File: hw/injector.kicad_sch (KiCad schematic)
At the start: 49 parts, among them Q401 150V N-ch, logic-level, Q402 150V N-ch, 18A peak, Q403 60V N-ch, 18A, Q404 150V N-ch, 18A peak, Q405 60V N-ch, 18A, Q406 150V N-ch, 18A peak, Q407 60V small-signal, Q408 150V N-ch, 18A peak, Q409 60V small-signal, Q410 150V N-ch, 18A peak, Q411 60V small-signal, U401 TPS40210

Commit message: Choose the gate drivers: AUIRS2181S on all eight gates, for having no interlock
Infineon AUIRS2181(4)S, datasheet retrieved and text-extracted. Its
first listed typical application is "Piezo / common rail Injection."

THE DECIDING PROPERTY IS ONE A PARAMETRIC SEARCH WOULD NEVER FILTER FOR:
no cross-conduction interlock (the datasheet's own feature table: 2181
"no", 2183/2184 "yes"). In a half bridge, HO and LO together is
shoot-through and every driver prevents it -- so the reflex is that a
driver WITHOUT interlock is the less safe choice. In an injector stage
the "high" and "low" switches are not a half bridge. They are in series
with the coil and must BOTH be on for it to conduct at all. UCC27282-Q1
and UCC27712-Q1 have interlock and could not fire an injector.

It also clears the two ratings the obvious 120 V candidate fails, and
both are now executable in run_sim.py:

  UCC27211A-Q1 HB absolute maximum 120 V, against a bank node at
  103.8 V worst case plus 12 V of VB -- 4.1 V of headroom on an
  absolute maximum. AUIRS2181S: 625 V, 5.4x.

  UCC27211A-Q1 HS DC minimum -1 V, against D_fw dropping the bank node
  1.0-1.3 V below ground on EVERY hold off-time -- violated in normal
  operation, not in a fault. AUIRS2181S operates to -5 V, clear by
  3.7 V.

Five in use: four on injector, each pairing one high side with one low
side by package rather than by circuit, and one on metering_egr for its
low side, so the board carries one gate-driver part number.

THE KILL PATH MOVES TO HIN. The part has no shutdown pin and a
ground-referenced FET cannot short a gate floating 100 V up -- but HIN
is ground-referenced, so supervisor.cir's kill FET goes there behind a
1k from the MCU. Slower than the low-side gate clamp (330 ns max driver
turn-off against 23 ns), which is acceptable because it is not the path
the fail-safe argument rests on: the low sides are in series with every
coil, and killing any one stops that cylinder.

12V_GATE, A RAIL THE BOARD DID NOT HAVE. The driv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
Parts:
- removed D407: 150V 20A ultrafast, symbol Device:D
- removed Q406: 150V N-ch, 18A peak, symbol Device:Q_NMOS_GSD
- removed Q407: 60V small-signal, symbol Device:Q_NMOS_GSD
- added C408, C409, C410, C411, C412, C413, C414, C415: 1uF 25V, symbol Device:C
- added C416: 10uF 25V, symbol Device:C
- added D407: 13V, symbol Device:D_Zener
- added D410, D411, D412, D413, D414: 150V 20A ultrafast, symbol Device:D
- added Q406: NPN 160V, DPAK, symbol Device:Q_NPN_BCE
- added Q407: NPN small-signal, symbol Device:Q_NPN_BCE
- added Q412, Q414, Q416: 150V N-ch, 18A peak, symbol Device:Q_NMOS_GSD
- added Q413, Q415, Q417: 60V small-signal, symbol Device:Q_NMOS_GSD
- added R421, R423, R424, R425: 470R, symbol Device:R
- added R422: 100k, symbol Device:R
- added R426, R427: 5mOhm 2W 1%, symbol Device:R
- added U402, U403, U404, U405: AUIRS2181S, Package_SO:SOIC-8_3.9x4.9mm_P1.27mm, symbol ecu25kva:AUIRS2181S
- D403, D405: value 150V 20A ultrafast -> 200V 1A fast; Note BLOCKING, not freewheeling. Without it the battery FET's ow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 -> Bootstrap diode -- the driver has none built in. Blocks VB,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; Tag INJ-RECIRC -> (none)
- D404, D406: value 150V 20A ultrafast -> 200V 1A fast; Note Anode to GROUND, cathode to the bank node. This is the slow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 -> Bootstrap diode -- the driver has none built in. Blocks VB,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; Source injector_turnoff.cir D_fw -> (none); Tag INJ-RECIRC -> (none)
- D408: Note Low side back into the boost reservoir. NOT a Zener active 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 -> BLOCKING, not freewheeling. Without it the battery FET's ow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; Peak 28.7 W instantaneous during turn-off, ~8x the 3.6 W average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 -> (none); Source injector_turnoff.cir Drc -- the diode memo 10 recommends an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 -> (none); Tag (none) -> INJ-RECIRC
- D409: Note Low side back into the boost reservoir. NOT a Zener active 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 -> Anode to GROUND, cathode to the bank node. This is the slow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; Peak 28.7 W instantaneous during turn-off, ~8x the 3.6 W average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 -> (none); Source injector_turnoff.cir Drc -- the diode memo 10 recommends an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 -> injector_turnoff.cir D_fw; Tag (none) -> INJ-RECIRC
- Q402: value 150V N-ch, 18A peak -> 60V small-signal; Note Bank-shared: cylinders 1 and 3 fire 240 crank degrees apart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 -> Pulls HIN low against a hung MCU driving it high through th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; Source injector_boost.cir -- the 100 V branch; injector_turnoff.ci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 -> supervisor.cir -- the kill FET, moved to the driver's logic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; Vds 150 V class against a 100 V rail the recirculation bump can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 -> (none)
- Q403, Q405: value 60V N-ch, 18A -> 60V small-signal; Note Chops for hold. 60 V class, not 150 V: the series blocking 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 -> Pulls HIN low against a hung MCU driving it high through th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; Source boost_converter.cir arrangement A -- hold current comes fro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 -> supervisor.cir -- the kill FET, moved to the driver's logic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; Vds 60 V -> (none)
- Q404: value 150V N-ch, 18A peak -> 60V small-signal; Note One cylinder in this bank. Kept as a separate switch rather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 -> Pulls HIN low against a hung MCU driving it high through th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; Source injector_boost.cir -- the 100 V branch; injector_turnoff.ci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 -> supervisor.cir -- the kill FET, moved to the driver's logic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; Vds 150 V class against a 100 V rail the recirculation bump can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 -> (none)
- Q408: Note Cylinder 3. Independent per channel -- the high side is ban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 -> Bank-shared: cylinders 1 and 3 fire 240 crank degrees apart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; Source injector_turnoff.cir Sls (Ron 20 mOhm) -> injector_boost.cir -- the 100 V branch; injector_turnoff.ci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; Vds 150 V class: at turn-off this drain is driven above the 100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 -> 150 V class against a 100 V rail the recirculation bump can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
- Q409, Q411: value 60V small-signal -> 60V N-ch, 18A; Note In parallel with the 470 ohm pulldown, not instead of it. R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 -> Chops for hold. 60 V class, not 150 V: the series blocking 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; Source supervisor.cir -- the kill FET -> boost_converter.cir arrangement A -- hold current comes fro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; Vds (none) -> 60 V
- Q410: Note Cylinder 2. Independent per channel -- the high side is ban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 -> One cylinder in this bank. Kept as a separate switch rather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; Source injector_turnoff.cir Sls (Ron 20 mOhm) -> injector_boost.cir -- the 100 V branch; injector_turnoff.ci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; Vds 150 V class: at turn-off this drain is driven above the 100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 -> 150 V class against a 100 V rail the recirculation bump can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
- R410, R411, R413: value 470R -> 1k; Note A pulldown to GROUND here would hold Vgs at minus the bank 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 -> Between the MCU and HIN, so the kill FET below can override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; Source supervisor.cir claim 6, referenced to SOURCE rather than to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 -> (none)
- R412: value 100k -> 1k; Note Bleed. With both high sides off and the low sides off, noth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 -> Between the MCU and HIN, so the kill FET below can override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
- R414: value 470R -> 47k; Note A pulldown to GROUND here would hold Vgs at minus the bank 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 -> Zener bias, split in two so neither resistor carries the fu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; Source supervisor.cir claim 6, referenced to SOURCE rather than to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 -> (none)
- R415: value 100k -> 47k; Note Bleed. With both high sides off and the low sides off, noth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 -> Second half.
- R416: value 470R -> 56R; Cost 21.3 mA per gate at 10 V; 1.28 W across all six -> (none); Note Largest standard value holding the gate under Vgs(th)=1.0 V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 -> The limit's sense resistor. 0.28 V drop at the 5 mA design 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; Source supervisor.cir claim 6; bom_requirements GATE-PULLDOWN -> (none)
- R417, R418: Cost 21.3 mA per gate at 10 V; 1.28 W across all six -> (none); Note Largest standard value holding the gate under Vgs(th)=1.0 V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 -> A pulldown to GROUND here would hold Vgs at minus the bank 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; Source supervisor.cir claim 6; bom_requirements GATE-PULLDOWN -> supervisor.cir claim 6, referenced to SOURCE rather than to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
- R419: value 5mOhm 2W 1% -> 100k; Note Bank A, cylinders 1 and 3 sharing one return. They fire 240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 -> Bleed. With both high sides off and the low sides off, noth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; Power 1.62 W at peak, but ~1.25% duty per cylinder at 1500 rpm -> (none); Signal 90 mV at the 18 A peak, 50 mV at the 10 A hold -- too small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 -> (none); Source settled on this sheet -- docs/pinmap.md sec.1.6 asked for t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 -> (none)
- R420: value 5mOhm 2W 1% -> 470R; Note Bank B, cylinder 2 alone. Drawn as its own shunt rather tha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 -> A pulldown to GROUND here would hold Vgs at minus the bank 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; Power 1.62 W at peak, but ~1.25% duty per cylinder at 1500 rpm -> (none); Signal 90 mV at the 18 A peak, 50 mV at the 10 A hold -- too small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 -> (none); Source settled on this sheet -- docs/pinmap.md sec.1.6 asked for t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 -> supervisor.cir claim 6, referenced to SOURCE rather than to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
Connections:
- net BOOST_100V: now also Q408.3 (D), Q410.3 (D), R414.1, D412.1 (K), D413.1 (K), D414.1 (K), Q406.2 (C); no longer D408.1 (K), D409.1 (K), Q402.3 (D), Q404.3 (D)
- net GATE_KILL: now also Q402.1 (G), Q403.1 (G), Q404.1 (G), Q405.1 (G), Q413.1 (G), Q415.1 (G), Q417.1 (G); no longer Q409.1 (G), Q411.1 (G)
- net GND: now also D409.2 (A), Q402.2 (S), Q403.2 (S), Q404.2 (S), Q405.2 (S), C409.2, C411.2, C413.2, C415.2, C416.2, D407.2 (A), D411.2 (A), Q413.2 (S), Q415.2 (S), Q417.2 (S), R422.2, R423.2, R424.2, R425.2, R426.2, R427.2, U402.3 (COM), U403.3 (COM), U404.3 (COM), U405.2 (LIN), U405.3 (COM); no longer D404.2 (A), D406.2 (A), Q409.2 (S), Q411.2 (S), R412.2, R415.2, R416.2, R417.2, R418.2, R420.2
- net HSA_BAT_GATE: now also Q409.1 (G), R418.1, U403.7 (HO); no longer Q403.1 (G), R411.1
- net HSA_BOOST_GATE: now also Q408.1 (G), R417.1, U402.7 (HO); no longer Q402.1 (G), R410.1
- net HSB_BAT_GATE: now also Q411.1 (G), R421.1, U405.7 (HO); no longer Q405.1 (G), R414.1
- net HSB_BOOST_GATE: now also Q410.1 (G), R420.1, U404.7 (HO); no longer Q404.1 (G), R413.1
- net INJ_A_03: now also D409.1 (K), Q408.2 (S), Q409.2 (S), R417.2, R418.2, R419.1, C408.2, C410.2, U402.6 (VS), U403.6 (VS); no longer D404.1 (K), Q402.2 (S), Q403.2 (S), R410.2, R411.2, R412.1
- net INJ_B_05: now also Q410.2 (S), Q411.2 (S), R420.2, C412.2, C414.2, D411.1 (K), R421.2, R422.1, U404.6 (VS), U405.6 (VS); no longer D406.1 (K), Q404.2 (S), Q405.2 (S), R413.2, R414.2, R415.1
- net INJ_HS_A: now also R410.1
- net INJ_HS_A_BAT: now also R411.1
- net INJ_HS_B: now also R412.1
- net INJ_HS_B_BAT: now also R413.1
- net INJ_LS1_73: now also D412.2 (A), Q412.3 (D)
- net INJ_LS2_29: now also D414.2 (A), Q416.3 (D); no longer D409.2 (A), Q410.3 (D)
- net INJ_LS3_07: now also D413.2 (A), Q414.3 (D); no longer D408.2 (A), Q408.3 (D)
- net INJ_LS_1: now also U402.2 (LIN)
- net INJ_LS_2: now also U404.2 (LIN)
- net INJ_LS_3: now also U403.2 (LIN)
- net ISNS_INJ_A_SENSE: now also Q412.2 (S), Q414.2 (S), R426.1; no longer Q408.2 (S), R419.1
- net ISNS_INJ_B_SENSE: now also Q416.2 (S), R427.1; no longer Q410.2 (S), R420.1
- net LS1_GATE: now also Q412.1 (G), Q413.3 (D), R423.1, U402.4 (LO); no longer R416.1
- net LS2_GATE: now also Q416.1 (G), Q417.3 (D), R425.1, U404.4 (LO); no longer Q410.1 (G), Q411.3 (D), R418.1
- net LS3_GATE: now also Q414.1 (G), Q415.3 (D), R424.1, U403.4 (LO); no longer Q408.1 (G), Q409.3 (D), R417.1
- net VBAT_PROT: now also D408.2 (A), D410.2 (A); no longer D403.2 (A), D405.2 (A)
- net UB1_VB: now reaches D405.1 (K)
- net UB1_VB: now also C412.1, U404.8 (VB); no longer Q405.3 (D)
- net UA1_VB: now reaches D403.1 (K)
- net UA1_VB: now also C408.1, U402.8 (VB); no longer Q403.3 (D)
- new net: D410.1 (K), Q411.3 (D)
- new net: D408.1 (K), Q409.3 (D)
- new net: R414.2, R415.1
- new net 12V_GATE: C409.1, C411.1, C413.1, C415.1, C416.1, D403.2 (A), D404.2 (A), D405.2 (A), D406.2 (A), Q407.3 (E), R416.2, U402.5 (VCC), U403.5 (VCC), U404.5 (VCC), U405.5 (VCC)
- new net BASE_12V: D407.1 (K), Q406.1 (B), Q407.2 (C), R415.2
- new net Q1E_12V: Q406.3 (E), Q407.1 (B), R416.1
- new net UA1_HIN: Q402.3 (D), R410.2, U402.1 (HIN)
- new net UA2_HIN: Q403.3 (D), R411.2, U403.1 (HIN)
- new net UA2_VB: C410.1, D404.1 (K), U403.8 (VB)
- new net UB1_HIN: Q404.3 (D), R412.2, U404.1 (HIN)
- new net UB2_HIN: Q405.3 (D), R413.2, U405.1 (HIN)
- new net UB2_VB: C414.1, D406.1 (K), U405.8 (VB)
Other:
- note added: "12V_GATE -- gate-drive supply for every driver on the board, from the boost rail so it survives cranking"
- note added: "GATE DRIVERS -- AUIRS2181S x4. Each pairs one high side with one low side; the pairing is by package, not by circuit."
- note added: "GATE DRIVERS: AUIRS2181S x4, chosen 21 Sep 2026. Its first listed application is 'Piezo / common rail Injection', and three properties decided it, each against a part that failed on it. NO CROSS-CONDUCTION INTERLOCK: in a half bridge HO and LO together is shoot-through, but here the high and low switches are in SERIES with the coil and must BOTH be on to fire it -- UCC27282-Q1 and UCC27712-Q1 hav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"
- note added: "GATE_KILL reaches the four high sides at the drivers' HIN inputs, not at the gates -- a ground-referenced kill FET cannot short a gate floating 100 V up, but HIN is ground-referenced. See the gate-driver block on the right."
- note removed: "GATE_KILL reaches the four high sides through the driver's own SHUTDOWN input, not through a clamp -- a ground-referenced kill FET cannot short a gate that floats 100 V up. Nothing is drawn for it here because the driver is not chosen; see the note at the foot of the sheet."
- note removed: "PARTS NOT CHOSEN ON THIS SHEET. Seven gate drivers and two current-sense amplifiers, on the same named-net treatment power_input gives its two controller gates. LOW-SIDE DRIVERS (LS1/LS2/LS3_DRV_IN -> *_GATE). Output impedance <= 25 ohm, from supervisor.cir claim 2: the 470 ohm pulldown is not a perturbation on the driver, it is the bottom half of a divider with it, and at 100 ohm the gate reache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"

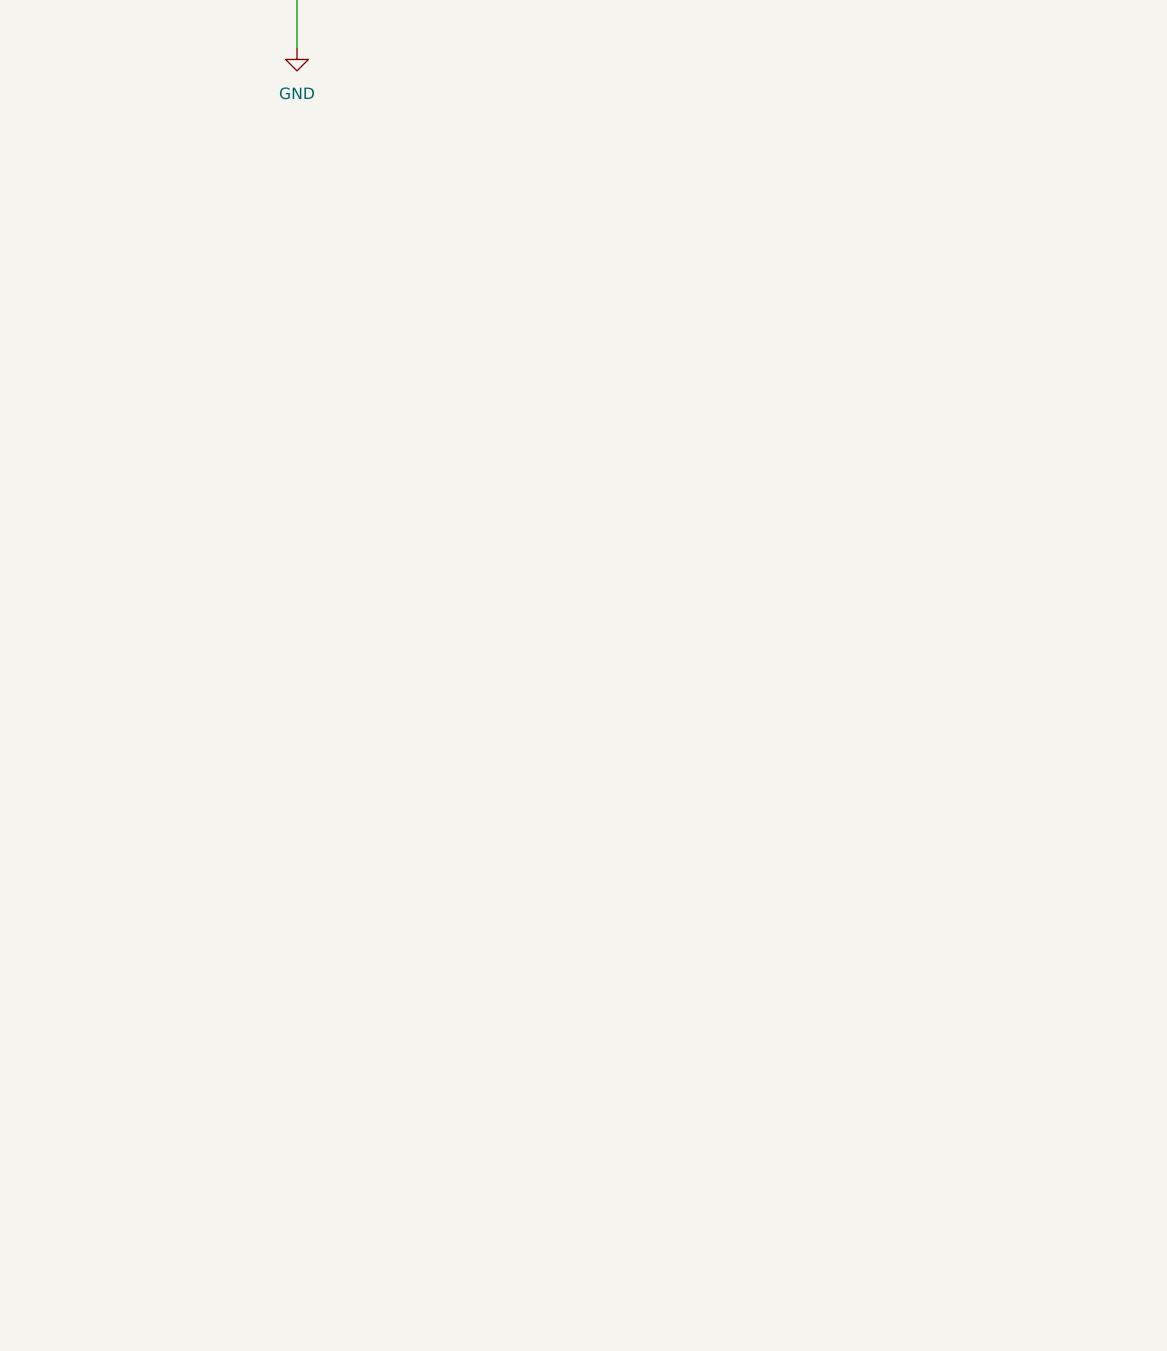
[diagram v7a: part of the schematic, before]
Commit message: Choose the current-sense amplifiers: INA181A1-Q1 on all three channels
TI SLYS018F, retrieved and text-extracted. VCM -0.2 V to 26 V, so it
sits across a ground-referenced shunt; gain 20; 350 kHz; +/-150 uV
offset at VCM = 0.

One part, one gain, three channels, and the gain is set for the
injector: 5 mOhm x 18 A x 20 = 1.80 V at the peak, 1.00 V at the 10 A
hold, leaving headroom to 3.28 V -- so a fault current up to 32.8 A is
MEASURED rather than clipped, which is what an overcurrent check needs.
The metering channel takes the same gain and reads its 0.675 A setpoint
at 675 mV, 844 counts.

Supplied from 3V3_MCU, which makes the output ADC-safe by construction:
it cannot swing above VS - 0.02 V, so these three channels need no
3.3 V zener at the MCU pin, unlike every channel on sensors_analog.

Closes MU-ISENSE's open half -- that tag specified the 50 mOhm shunt and
said the amplifier was not optional. The Kelvin-tap layout requirement
is carried in each amplifier's own field.

Also redrawn: the metering FET, placed at rot=270 since 20 September.
At 270 the drain and source sit side by side and every wire to a rail
above or below comes out diagonal -- the same drawing bug the injector
sheet had and fixed first. The netlist was always right; the page was
not.

Open ends 12 -> 9. 24/24 blocks, 24/24 netlist checks, 36 supply pins
all decoupled.

Co-Authored-By: Claude Opus 5 <noreply@anthropic.com>
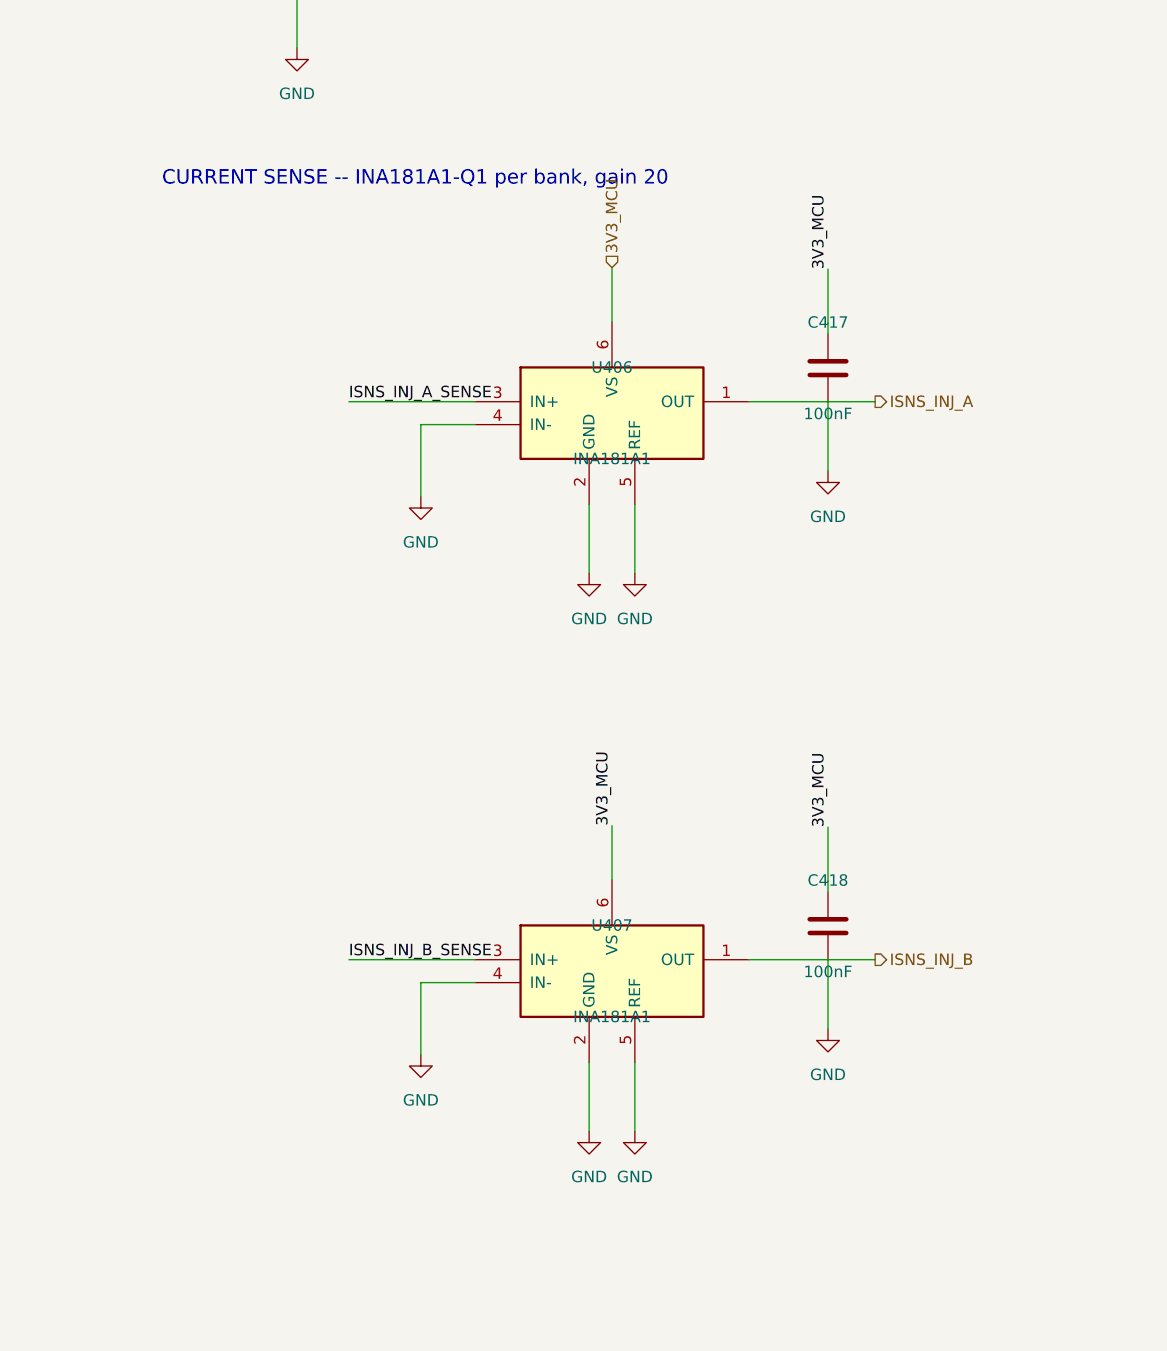
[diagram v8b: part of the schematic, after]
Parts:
- added C417, C418: 100nF, symbol Device:C
- added U406, U407: INA181A1, Package_TO_SOT_SMD:SOT-23-6, symbol ecu25kva:INA181A1
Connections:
- net GND: now also C417.2, C418.2, U406.2 (GND), U406.4 (IN-), U406.5 (REF), U407.2 (GND), U407.4 (IN-), U407.5 (REF)
- net ISNS_INJ_A_SENSE: now also U406.3 (IN+)
- net ISNS_INJ_B_SENSE: now also U407.3 (IN+)
- new net 3V3_MCU: C417.1, C418.1, U406.6 (VS), U407.6 (VS)
- new net ISNS_INJ_A: U406.1 (OUT)
- new net ISNS_INJ_B: U407.1 (OUT)
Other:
- note added: "CURRENT SENSE -- INA181A1-Q1 per bank, gain 20"
